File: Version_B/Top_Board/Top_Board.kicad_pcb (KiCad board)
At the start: 2 copper layers, 78.7 x 31 mm, 5 parts, among them J1 90_Deg_Conn, J2 90_Deg_Conn, U1 T-Display-S3

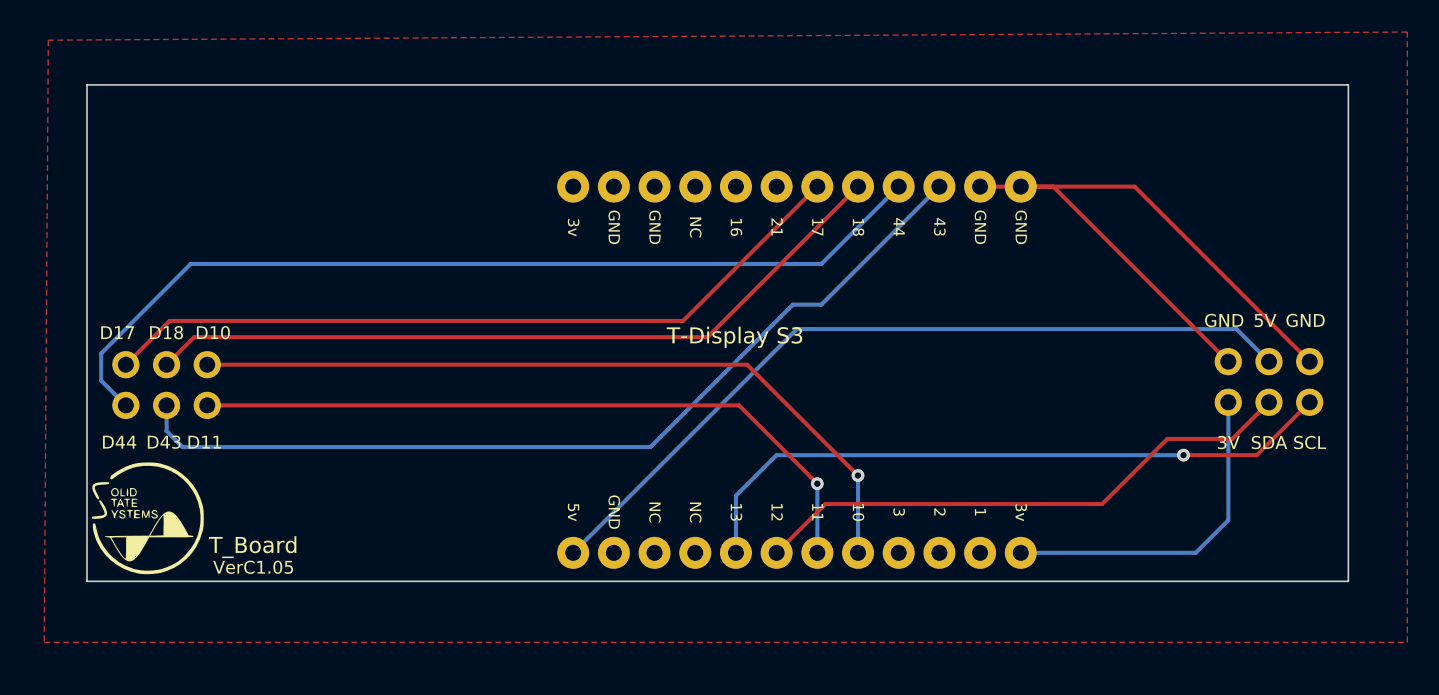
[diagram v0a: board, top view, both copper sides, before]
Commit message: fixed directory overwrite
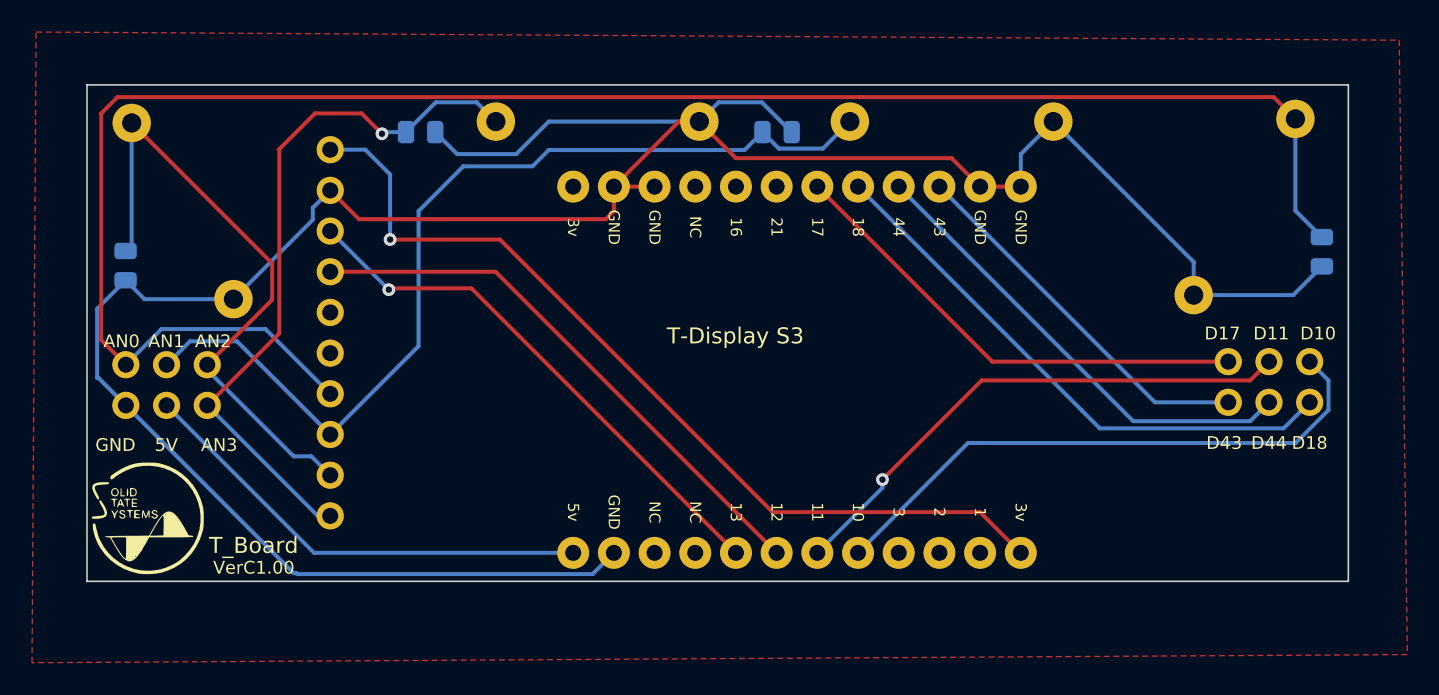
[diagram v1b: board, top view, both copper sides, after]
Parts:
- removed the G*** at (115.6, 80.5)
- added J2: ADS1015, Voltage_Sensor_Timer:PinSocket_1x10_P2.54mm_Vertical_1, B.Cu at (128.3, 105.6)
- added R1: R, Resistor_SMD:R_0805_2012Metric, B.Cu at (190.2, 89.2)
- added R2: R, Resistor_THT:R_Axial_DIN0411_L9.9mm_D3.6mm_P12.70mm_Horizontal, B.Cu at (188.6, 80.9)
- added R3: R, Resistor_THT:R_Axial_DIN0411_L9.9mm_D3.6mm_P12.70mm_Horizontal, B.Cu at (116.0, 81.1)
- added R4: R, Resistor_SMD:R_0805_2012Metric, B.Cu at (115.6, 90.0)
- added R5: R, Resistor_SMD:R_0805_2012Metric, B.Cu at (156.2, 81.7)
- added R6: R, Resistor_THT:R_Axial_DIN0411_L9.9mm_D3.6mm_P12.70mm_Horizontal, B.Cu at (160.8, 81.0)
- added R7: R, Resistor_SMD:R_0805_2012Metric, B.Cu at (134.0, 81.7)
- added R8: R, Resistor_THT:R_Axial_DIN0411_L9.9mm_D3.6mm_P12.70mm_Horizontal, B.Cu at (138.7, 81.0)
- renumbered J2 to J4
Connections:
- J1 pad 1: D17 -> AN0
- J1 pad 2: D44 -> GND
- J1 pad 3: D18 -> AN1
- J1 pad 4: D43 -> 5V
- J1 pad 5: D10 -> AN2
- J1 pad 6: D11 -> AN3
- J4 pad 1: GND -> D17
- J4 pad 2: 3V -> D43
- J4 pad 3: 5V -> D11
- J4 pad 4: SDA -> D44
- J4 pad 5: GND -> D10
- J4 pad 6: SCL -> D18
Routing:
- net GND: track 42.6 -> 165.8 mm
- net AN0: track 0.00 -> 115.3 mm
- net AN1: track 0.00 -> 59.6 mm
- net AN3: track 0.00 -> 44.7 mm, vias 0 -> 1
- net AN2: track 0.00 -> 39.3 mm
- net 3V: track 21.2 -> 55.9 mm, vias 0 -> 1
- net D43: track 57.0 -> 23.6 mm
- net D44: track 58.0 -> 29.7 mm
- net 5V: track 50.1 -> 29.2 mm
- net D17: track 47.8 -> 30.2 mm
- net D18: track 47.8 -> 35.1 mm
- net D10: track 48.3 -> 36.6 mm, vias 1 -> 0
- net D11: track 44.4 -> 33.4 mm
- net SCL: track 41.8 -> 33.7 mm
- net SDA: track 34.6 -> 35.1 mm
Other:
- board text added: "3.9 Mohm"
- board text added: "3.9 Mohms"
- board text added: "ADS1015"
- board text added: "AN0"
- board text added: "AN1"
- board text added: "AN2"
- board text added: "AN3"
- board text added: "D5"
- board text added: "VerC1.00"
- board text removed: "3V"
- board text removed: "SCL"
- board text removed: "SDA"
- board text removed: "VerC1.05"

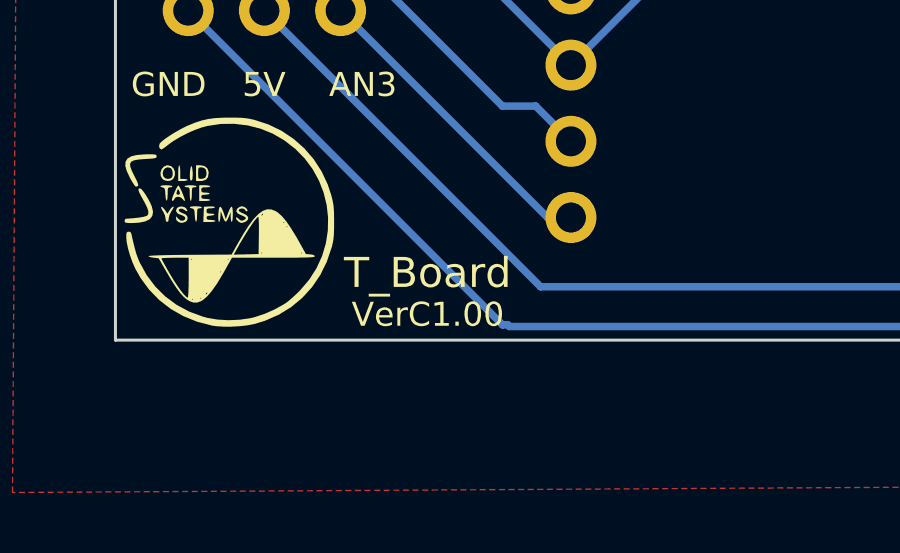
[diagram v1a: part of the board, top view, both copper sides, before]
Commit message: 90 degree terminal block added
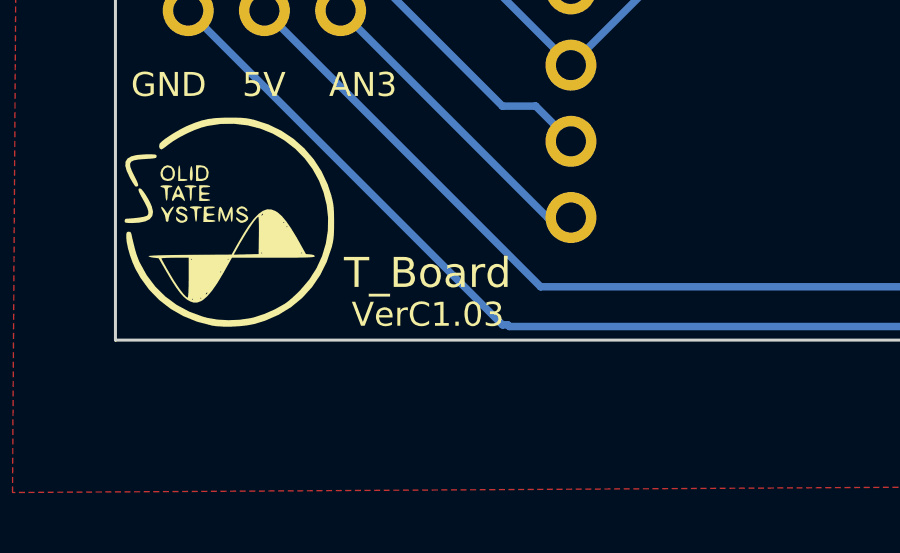
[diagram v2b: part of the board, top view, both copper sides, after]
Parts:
- R1, R2, R3, R4, R5, R6, R7, R8: value R -> 3.9M
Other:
- board text added: "VerC1.03"
- board text removed: "VerC1.00"
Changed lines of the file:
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@@
     (fp_arc (start -19.901865 15.815496) (mid -19.151865 16.565496) (end -19.901865 17.315496)
       (stroke (width 0.25) (type solid)) (layer "Dwgs.User"))
-    (fp_arc (start -2.503865 17.198296) (mid -3.253861 16.448296) (end -2.503865 15.698295)
+    (fp_arc (start -2.503865 17.198296) (mid -3.253859 16.448296) (end -2.503865 15.698295)
       (stroke (width 0.25) (type solid)) (layer "Dwgs.User"))
     (fp_arc (start -2.503864 17.498295) (mid -3.553865 16.448295) (end -2.503864 15.398295)
@@
         (effects (font (size 1 1) (thickness 0.15)) (justify mirror))
     )
-    (fp_text value "R" (at 6.35 -2.92 60) (layer "B.Fab") hide
+    (fp_text value "3.9M" (at 6.35 -2.92 60) (layer "B.Fab") hide
         (effects (font (size 1 1) (thickness 0.15)) (justify mirror))
     )
@@
         (effects (font (size 1 1) (thickness 0.15)) (justify mirror))
     )
-    (fp_text value "R" (at 0 -1.65 90) (layer "B.Fab") hide
+    (fp_text value "3.9M" (at 0 -1.65 90) (layer "B.Fab") hide
         (effects (font (size 1 1) (thickness 0.15)) (justify mirror))
     )
@@
         (effects (font (size 1 1) (thickness 0.15)) (justify mirror))
     )
-    (fp_text value "R" (at 0 -1.65) (layer "B.Fab")
+    (fp_text value "3.9M" (at 0 -1.65) (layer "B.Fab")
         (effects (font (size 1 1) (thickness 0.15)) (justify mirror))
     )
@@
         (effects (font (size 1 1) (thickness 0.15)) (justify mirror))
     )
-    (fp_text value "R" (at 4.318 -13.589 90) (layer "B.Fab") hide
+    (fp_text value "3.9M" (at 4.318 -13.589 90) (layer "B.Fab") hide
         (effects (font (size 1 1) (thickness 0.15)) (justify mirror))
     )
@@
         (effects (font (size 1 1) (thickness 0.15)) (justify mirror))
     )
-    (fp_text value "R" (at 6.35 -2.92 120) (layer "B.Fab") hide
+    (fp_text value "3.9M" (at 6.35 -2.92 120) (layer "B.Fab") hide
         (effects (font (size 1 1) (thickness 0.15)) (justify mirror))
     )
@@
         (effects (font (size 1 1) (thickness 0.15)) (justify mirror))
     )
-    (fp_text value "R" (at 6.35 -2.92) (layer "B.Fab")
+    (fp_text value "3.9M" (at 6.35 -2.92) (layer "B.Fab")
         (effects (font (size 1 1) (thickness 0.15)) (justify mirror))
     )
@@
         (effects (font (size 1 1) (thickness 0.15)) (justify mirror))
     )
-    (fp_text value "R" (at 0 -1.65) (layer "B.Fab")
+    (fp_text value "3.9M" (at 0 -1.65) (layer "B.Fab")
         (effects (font (size 1 1) (thickness 0.15)) (justify mirror))
     )
@@
         (effects (font (size 1 1) (thickness 0.15)) (justify mirror))
     )
-    (fp_text value "R" (at 6.35 -2.92) (layer "B.Fab")
+    (fp_text value "3.9M" (at 6.35 -2.92) (layer "B.Fab")
         (effects (font (size 1 1) (thickness 0.15)) (justify mirror))
     )
@@
     (effects (font (size 0.8 0.8) (thickness 0.15)))
   )
-  (gr_text "VerC1.00" (at 121.031 109.347) (layer "F.SilkS")
+  (gr_text "VerC1.03" (at 121.031 109.347) (layer "F.SilkS")
     (effects (font (size 0.8 0.8) (thickness 0.15)) (justify left bottom))
   )
@@
     (pts (xy 191.899218 109.728) (xy 113.159218 109.728))
     (height -13.462)
-    (gr_text "78.7400 mm" (at 152.529218 121.39) (layer "B.Cu")
+    (gr_text "3.1000 in" (at 152.529218 121.39) (layer "B.Cu")
       (effects (font (size 1.5 1.5) (thickness 0.3)))
     )
@@
     (pts (xy 113.159218 78.739553) (xy 113.159218 109.728))
     (height 11.559218)
-    (gr_text "30.9884 mm" (at 99.8 94.233777 90) (layer "Dwgs.User")
+    (gr_text "1.2200 in" (at 99.8 94.233777 90) (layer "Dwgs.User")
       (effects (font (size 1.5 1.5) (thickness 0.3)))
     )
@@
     (pts (xy 113.159218 78.739553) (xy 191.899218 78.739553))
     (height -12.572553)
-    (gr_text "78.7400 mm" (at 152.529218 64.367) (layer "User.1")
+    (gr_text "3.1000 in" (at 152.529218 64.367) (layer "User.1")
       (effects (font (size 1.5 1.5) (thickness 0.3)))
     )
@@
     (pts (xy 186.944 105.664) (xy 118.11 105.664))
     (height -11.811)
-    (gr_text "68.8340 mm" (at 152.527 116.325) (layer "User.1")
+    (gr_text "2.7100 in" (at 152.527 116.325) (layer "User.1")
       (effects (font (size 1 1) (thickness 0.15)))
     )
